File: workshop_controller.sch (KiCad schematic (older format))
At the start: 33 parts, among them J1 Conn_02x10_Odd_Even, J2 Conn_02x10_Odd_Even, J3 AudioJack3, J4 Micro_SD_Card, J5 Conn_02x25_Odd_Even, SW1 SW_Push, SW2 SW_Push, SW3 SW_Push, SW4 SW_Push, U1 MPU-9250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

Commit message: Add opamp for mic preamp
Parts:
- added U5, U6: LM358, Package_SO:MSOP-8_3x3mm_P0.65mm, symbol Amplifier_Operational:LM358
- J4: symbol Connector:Micro_SD_Card -> workshop_controller-rescue:Micro_SD_Card-Connector
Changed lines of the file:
@@
 EESchema Schematic File Version 4
 LIBS:workshop_controller-cache
-EELAYER 29 0
+EELAYER 26 0
 EELAYER END
 $Descr A4 11693 8268
@@
 $EndComp
 $Comp
-L Connector:Micro_SD_Card J4
+L workshop_controller-rescue:Micro_SD_Card-Connector J4
 U 1 1 5CCA02B7
 P 7450 1350
@@
 JOY_Y
 $Comp
-L power:GND #PWR?
+L power:GND #PWR0138
 U 1 1 5CD0AC46
 P 1100 1950
-F 0 "#PWR?" H 1100 1700 50  0001 C CNN
+F 0 "#PWR0138" H 1100 1700 50  0001 C CNN
 F 1 "GND" H 1105 1777 50  0000 C CNN
 F 2 "" H 1100 1950 50  0001 C CNN
@@
 $EndComp
 $Comp
-L power:GND #PWR?
+L power:GND #PWR0139
 U 1 1 5CD0AFBD
 P 1600 1950
-F 0 "#PWR?" H 1600 1700 50  0001 C CNN
+F 0 "#PWR0139" H 1600 1700 50  0001 C CNN
 F 1 "GND" H 1605 1777 50  0000 C CNN
 F 2 "" H 1600 1950 50  0001 C CNN
@@
 $EndComp
 $Comp
-L power:+3V3 #PWR?
+L power:+3V3 #PWR0140
 U 1 1 5CD0C0CF
 P 800 1950
-F 0 "#PWR?" H 800 1800 50  0001 C CNN
+F 0 "#PWR0140" H 800 1800 50  0001 C CNN
 F 1 "+3V3" H 815 2123 50  0000 C CNN
 F 2 "" H 800 1950 50  0001 C CNN
@@
 $EndComp
 $Comp
-L power:+3V3 #PWR?
+L power:+3V3 #PWR0141
 U 1 1 5CD0D40E
 P 1300 1950
-F 0 "#PWR?" H 1300 1800 50  0001 C CNN
+F 0 "#PWR0141" H 1300 1800 50  0001 C CNN
 F 1 "+3V3" H 1315 2123 50  0000 C CNN
 F 2 "" H 1300 1950 50  0001 C CNN
@@
 	-1   0    0    1
 $EndComp
+$Comp
+L Amplifier_Operational:LM358 U5
+U 1 1 5CABA90F
+P 1550 4800
+F 0 "U5" H 1550 5167 50  0000 C CNN
+F 1 "LM358" H 1550 5076 50  0000 C CNN
+F 2 "Package_SO:MSOP-8_3x3mm_P0.65mm" H 1550 4800 50  0001 C CNN
+F 3 "http://www.ti.com/lit/ds/symlink/lm2904-n.pdf" H 1550 4800 50  0001 C CNN
+	1    1550 4800
+	1    0    0    -1
+$EndComp
+$Comp
+L Amplifier_Operational:LM358 U6
+U 2 1 5CABABB9
+P 1050 5100
+F 0 "U6" H 1050 5467 50  0000 C CNN
+F 1 "LM358" H 1050 5376 50  0000 C CNN
+F 2 "Package_SO:MSOP-8_3x3mm_P0.65mm" H 1050 5100 50  0001 C CNN
+F 3 "http://www.ti.com/lit/ds/symlink/lm2904-n.pdf" H 1050 5100 50  0001 C CNN
+	2    1050 5100
+	1    0    0    -1
+$EndComp
+$Comp
+L Amplifier_Operational:LM358 U6
+U 3 1 5CABAC9F
+P 2050 4850
+F 0 "U6" H 2008 4896 50  0000 L CNN
+F 1 "LM358" H 2008 4805 50  0000 L CNN
+F 2 "Package_SO:MSOP-8_3x3mm_P0.65mm" H 2050 4850 50  0001 C CNN
+F 3 "http://www.ti.com/lit/ds/symlink/lm2904-n.pdf" H 2050 4850 50  0001 C CNN
+	3    2050 4850
+	1    0    0    -1
+$EndComp
 $EndSCHEMATC

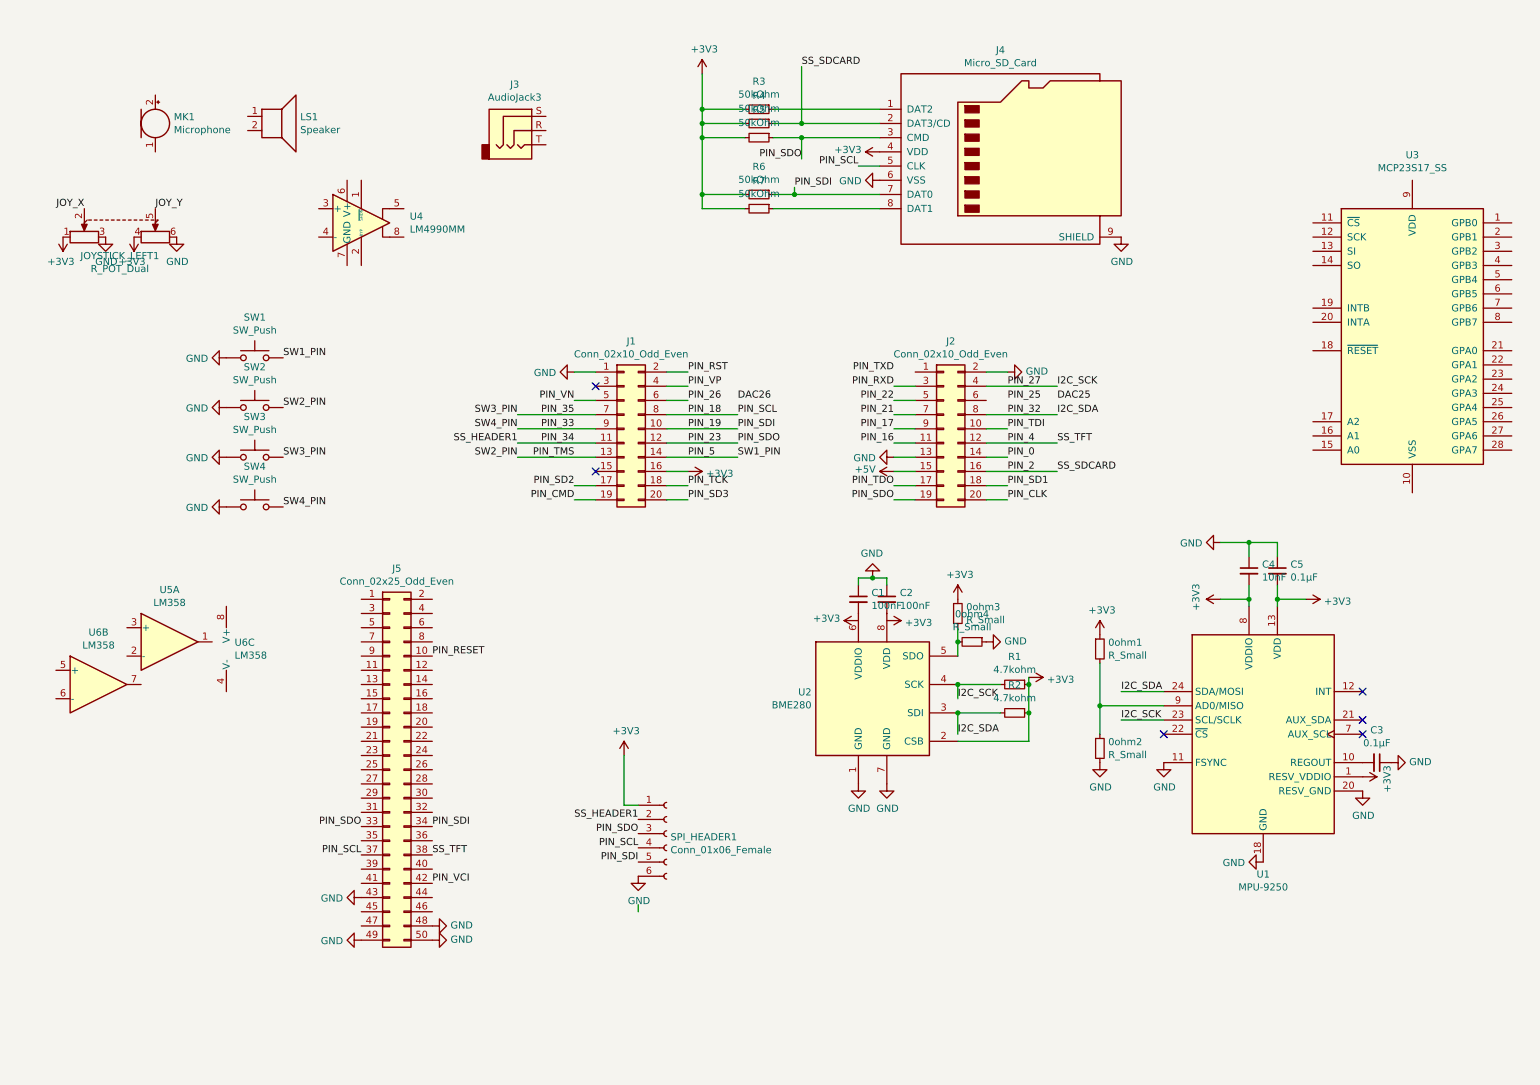
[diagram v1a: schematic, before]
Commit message: Add microphone circuit
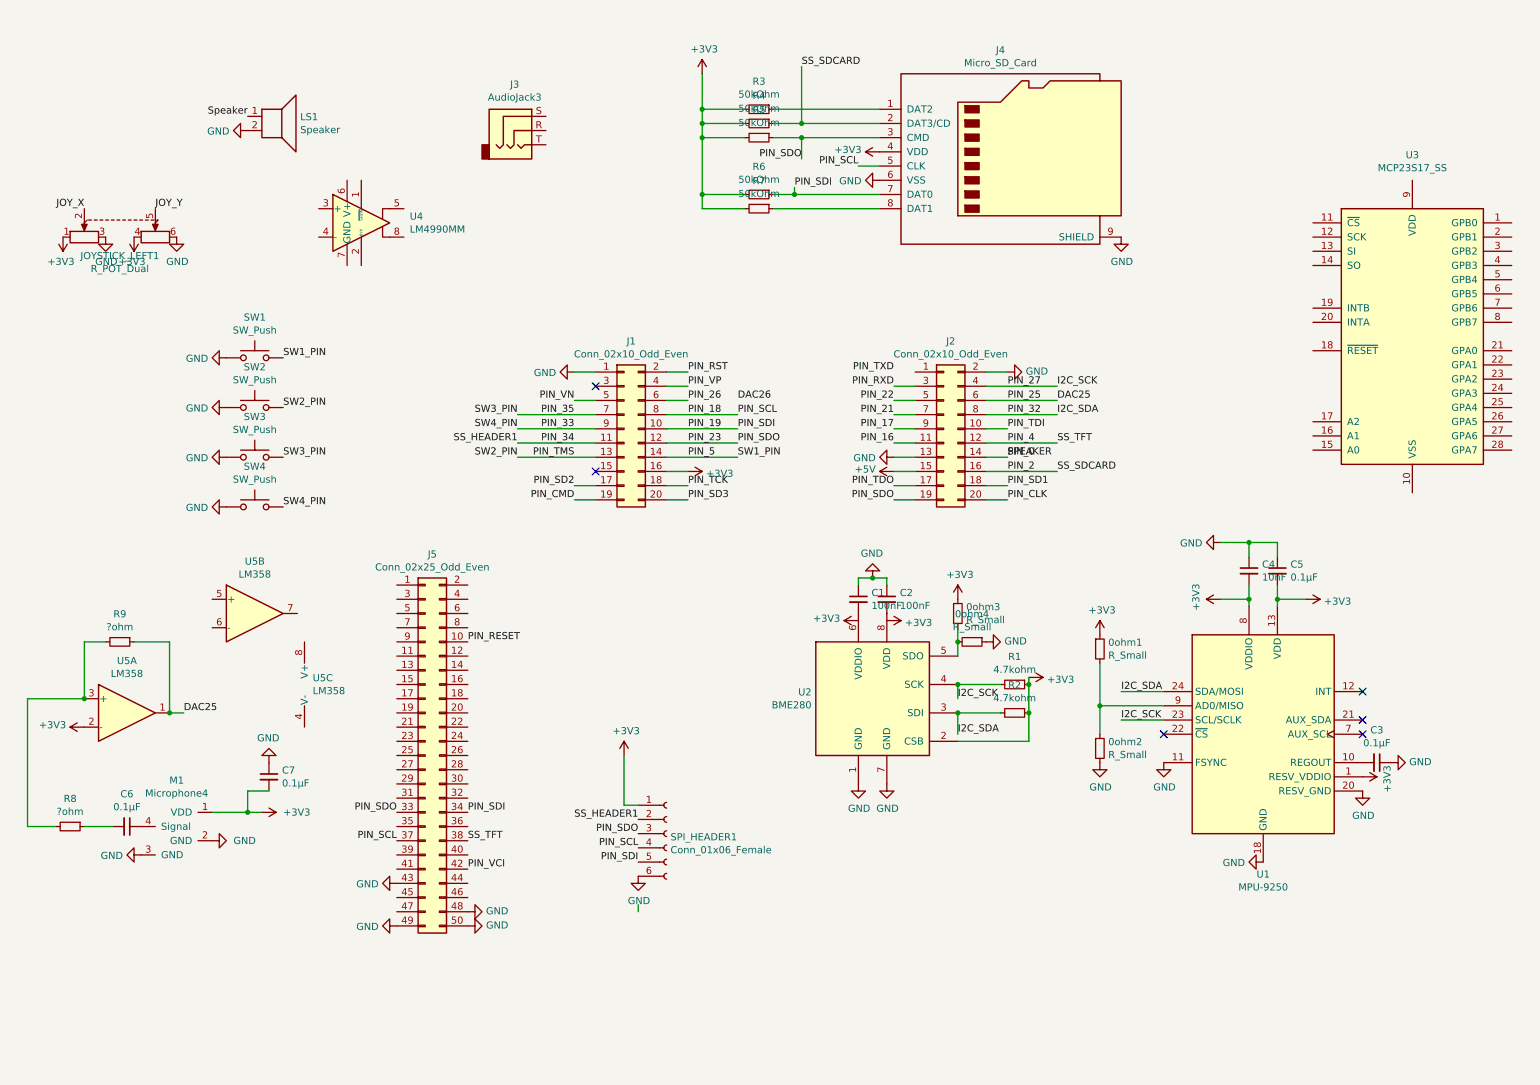
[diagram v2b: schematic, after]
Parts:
- removed MK1: Microphone, symbol Device:Microphone
- removed U6: LM358, Package_SO:MSOP-8_3x3mm_P0.65mm, symbol Amplifier_Operational:LM358
- added C6, C7: 0.1µF, Capacitor_SMD:C_0603_1608Metric_Pad1.05x0.95mm_HandSolder, symbol Device:C_Small
- added M1: Microphone4, Hackheim_logo:CMM-3125AT-42316-TR, symbol bytebarista:Microphone4
- added R8, R9: ?ohm, Resistor_SMD:R_0603_1608Metric_Pad1.05x0.95mm_HandSolder, symbol Device:R_Small
- added unit 2 of U5
- added unit 3 of U5
- LS1: footprint (none) -> Hackheim_logo:Speaker_SMD_CUI
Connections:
- net +3V3: now also U5.2 (-), C7.2, M1.1 (VDD)
- net DAC25: now also J2.6 (Pin_6), U5.1, R9.1
- net GND: now also LS1.2, C7.1, M1.2 (GND), M1.3 (GND)
- net Speaker: now reaches LS1.1
- net at U5.3 (+): now also R8.2, R9.2
- new net: C6.1, M1.4 (Signal)
- new net: C6.2, R8.1
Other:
- moved on the sheet: J5

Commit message: Wire BME280
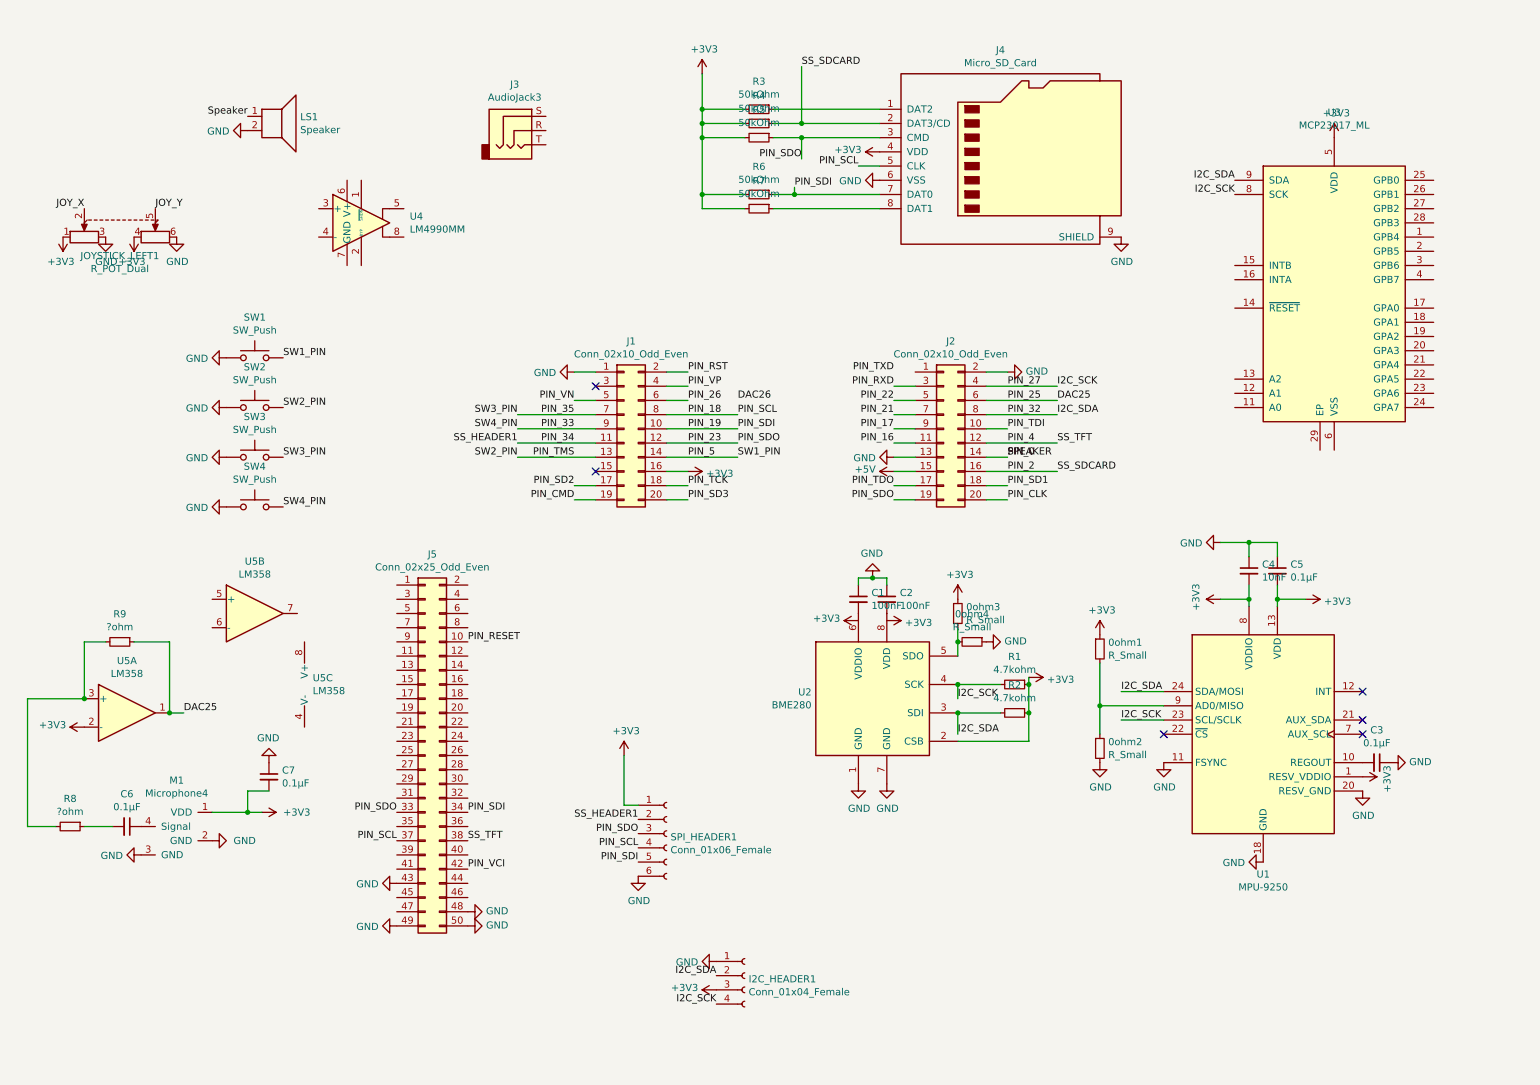
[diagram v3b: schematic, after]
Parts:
- removed U3: MCP23S17_SS, Package_SO:SSOP-28_5.3x10.2mm_P0.65mm, symbol Interface_Expansion:MCP23S17_SS
- added I2C_HEADER1: Conn_01x04_Female, symbol Connector:Conn_01x04_Female
- added U3: MCP23017_ML, Package_DFN_QFN:QFN-28-1EP_6x6mm_P0.65mm_EP4.25x4.25mm, symbol Interface_Expansion:MCP23017_ML
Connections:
- net +3V3: now also I2C_HEADER1.3 (Pin_3), U3.5 (VDD)
- net GND: now also I2C_HEADER1.1 (Pin_1)
- net I2C_SCK: now also I2C_HEADER1.4 (Pin_4), U3.8 (SCK)
- net I2C_SDA: now also I2C_HEADER1.2 (Pin_2), U3.9 (SDA)
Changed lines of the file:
@@
-$EndComp
-$Comp
-L Interface_Expansion:MCP23S17_SS U3
-U 1 1 5CA69BB7
-P 10300 2650
-F 0 "U3" H 10300 3928 50  0000 C CNN
-F 1 "MCP23S17_SS" H 10300 3837 50  0000 C CNN
-F 2 "Package_SO:SSOP-28_5.3x10.2mm_P0.65mm" H 10500 1650 50  0001 L CNN
-F 3 "http://ww1.microchip.com/downloads/en/DeviceDoc/20001952C.pdf" H 10500 1550 50  0001 L CNN
-	1    10300 2650
-	1    0    0    -1
 $EndComp
 $Comp
@@
 Text Label 3650 6400 0    50   ~ 0
 PIN_VCI
-Wire Wire Line
-	4850 6650 4850 6700
 $Comp
 L Amplifier_Audio:LM4990MM U4
@@
 Wire Wire Line
 	1150 6100 950  6100
+$Comp
+L Interface_Expansion:MCP23017_ML U3
+U 1 1 5CB50D6F
+P 9750 2350
+F 0 "U3" H 9750 3628 50  0000 C CNN
+F 1 "MCP23017_ML" H 9750 3537 50  0000 C CNN
+F 2 "Package_DFN_QFN:QFN-28-1EP_6x6mm_P0.65mm_EP4.25x4.25mm" H 9950 1350 50  0001 L CNN
+F 3 "http://ww1.microchip.com/downloads/en/DeviceDoc/20001952C.pdf" H 9950 1250 50  0001 L CNN
+	1    9750 2350
+	1    0    0    -1
+$EndComp
+Text Label 9050 1550 2    50   ~ 0
+I2C_SDA
+Text Label 9050 1650 2    50   ~ 0
+I2C_SCK
+$Comp
+L power:+3V3 #PWR0148
+U 1 1 5CB510D4
+P 9750 1250
+F 0 "#PWR0148" H 9750 1100 50  0001 C CNN
+F 1 "+3V3" H 9765 1423 50  0000 C CNN
+F 2 "" H 9750 1250 50  0001 C CNN
+F 3 "" H 9750 1250 50  0001 C CNN
+	1    9750 1250
+	1    0    0    -1
+$EndComp
+$Comp
+L Connector:Conn_01x04_Female I2C_HEADER1
+U 1 1 5CB520FF
+P 5600 7150
+F 0 "I2C_HEADER1" H 5627 7126 50  0000 L CNN
+F 1 "Conn_01x04_Female" H 5627 7035 50  0000 L CNN
+F 2 "" H 5600 7150 50  0001 C CNN
+F 3 "~" H 5600 7150 50  0001 C CNN
+	1    5600 7150
+	1    0    0    -1
+$EndComp
+$Comp
+L power:GND #PWR?
+U 1 1 5CB52403
+P 5400 7050
+F 0 "#PWR?" H 5400 6800 50  0001 C CNN
+F 1 "GND" V 5405 6922 50  0000 R CNN
+F 2 "" H 5400 7050 50  0001 C CNN
+F 3 "" H 5400 7050 50  0001 C CNN
+	1    5400 7050
+	0    1    1    0
+$EndComp
+Text Label 5400 7150 2    50   ~ 0
+I2C_SDA
+$Comp
+L power:+3V3 #PWR?
+U 1 1 5CB527A9
+P 5400 7250
+F 0 "#PWR?" H 5400 7100 50  0001 C CNN
+F 1 "+3V3" V 5415 7378 50  0000 L CNN
+F 2 "" H 5400 7250 50  0001 C CNN
+F 3 "" H 5400 7250 50  0001 C CNN
+	1    5400 7250
+	0    -1   -1   0
+$EndComp
+Text Label 5400 7350 2    50   ~ 0
+I2C_SCK
 $EndSCHEMATC

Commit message: Update schematic
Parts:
- renumbered 0ohm3 to R10, 0ohm4 to R11, 0ohm1 to R12, 0ohm2 to R13
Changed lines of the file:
@@
 NoConn ~ 8550 5450
 $Comp
-L Device:R_Small 0ohm1
+L Device:R_Small R12
 U 1 1 5CB08528
 P 8100 4850
-F 0 "0ohm1" H 8159 4896 50  0000 L CNN
+F 0 "R12" H 8159 4896 50  0000 L CNN
 F 1 "R_Small" H 8159 4805 50  0000 L CNN
 F 2 "Resistor_SMD:R_0603_1608Metric_Pad1.05x0.95mm_HandSolder" H 8100 4850 50  0001 C CNN
@@
 $EndComp
 $Comp
-L Device:R_Small 0ohm2
+L Device:R_Small R13
 U 1 1 5CB085A3
 P 8100 5550
-F 0 "0ohm2" H 8159 5596 50  0000 L CNN
+F 0 "R13" H 8159 5596 50  0000 L CNN
 F 1 "R_Small" H 8159 5505 50  0000 L CNN
 F 2 "Resistor_SMD:R_0603_1608Metric_Pad1.05x0.95mm_HandSolder" H 8100 5550 50  0001 C CNN
@@
 $EndComp
 $Comp
-L Device:R_Small 0ohm3
+L Device:R_Small R10
 U 1 1 5CB6002C
 P 7100 4600
-F 0 "0ohm3" H 7159 4646 50  0000 L CNN
+F 0 "R10" H 7159 4646 50  0000 L CNN
 F 1 "R_Small" H 7159 4555 50  0000 L CNN
 F 2 "Resistor_SMD:R_0603_1608Metric_Pad1.05x0.95mm_HandSolder" H 7100 4600 50  0001 C CNN
@@
 $EndComp
 $Comp
-L Device:R_Small 0ohm4
+L Device:R_Small R11
 U 1 1 5CB80FEA
 P 7200 4800
-F 0 "0ohm4" V 7004 4800 50  0000 C CNN
+F 0 "R11" V 7004 4800 50  0000 C CNN
 F 1 "R_Small" V 7095 4800 50  0000 C CNN
 F 2 "Resistor_SMD:R_0603_1608Metric_Pad1.05x0.95mm_HandSolder" H 7200 4800 50  0001 C CNN
@@
 	0    1    1    0
 $EndComp
-Wire Wire Line
-	7100 4700 7100 4800
-Connection ~ 7100 4800
-Wire Wire Line
-	7100 4800 7100 4900
 $Comp
 L power:+3V3 #PWR0129
@@
 $EndComp
 $Comp
-L power:GND #PWR?
+L power:GND #PWR0149
 U 1 1 5CB52403
 P 5400 7050
-F 0 "#PWR?" H 5400 6800 50  0001 C CNN
+F 0 "#PWR0149" H 5400 6800 50  0001 C CNN
 F 1 "GND" V 5405 6922 50  0000 R CNN
 F 2 "" H 5400 7050 50  0001 C CNN
@@
 I2C_SDA
 $Comp
-L power:+3V3 #PWR?
+L power:+3V3 #PWR0150
 U 1 1 5CB527A9
 P 5400 7250
-F 0 "#PWR?" H 5400 7100 50  0001 C CNN
+F 0 "#PWR0150" H 5400 7100 50  0001 C CNN
 F 1 "+3V3" V 5415 7378 50  0000 L CNN
 F 2 "" H 5400 7250 50  0001 C CNN
@@
 Text Label 5400 7350 2    50   ~ 0
 I2C_SCK
+Connection ~ 7100 4800
+Wire Wire Line
+	7100 4800 7100 4900
+Wire Wire Line
+	7100 4700 7100 4800
 $EndSCHEMATC

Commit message: Wire components
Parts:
- I2C_HEADER1: footprint (none) -> Connector_PinHeader_2.54mm:PinHeader_1x04_P2.54mm_Horizontal
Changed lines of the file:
@@
 F 0 "I2C_HEADER1" H 5627 7126 50  0000 L CNN
 F 1 "Conn_01x04_Female" H 5627 7035 50  0000 L CNN
-F 2 "" H 5600 7150 50  0001 C CNN
+F 2 "Connector_PinHeader_2.54mm:PinHeader_1x04_P2.54mm_Horizontal" H 5600 7150 50  0001 C CNN
 F 3 "~" H 5600 7150 50  0001 C CNN
 	1    5600 7150

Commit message: Connect mpu9250, speaker circuit and gpio extender
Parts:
- removed U4: LM4990MM, Package_SO:TSSOP-8_3x3mm_P0.65mm, symbol Amplifier_Audio:LM4990MM
- added C10, C8, C9: C_Small, Capacitor_SMD:C_0603_1608Metric_Pad1.05x0.95mm_HandSolder, symbol Device:C_Small
- added C11: CP1_Small, Capacitor_SMD:C_0603_1608Metric_Pad1.05x0.95mm_HandSolder, symbol Device:CP1_Small
- added R14, R15, R16, R17: R_Small, Resistor_SMD:R_0603_1608Metric_Pad1.05x0.95mm_HandSolder, symbol Device:R_Small
- added U4: TPA6203A1, Package_SO:MSOP-8_3x3mm_P0.65mm, symbol bytebarista:TPA6203A1
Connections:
- net labels added: PIN_AMP_SHUTDOWN, PIN_DAC1, PIN_DAC2
- net labels removed: Speaker
- wire segments 103 -> 127
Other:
- moved on the sheet: JOYSTICK_LEFT1, LS1
